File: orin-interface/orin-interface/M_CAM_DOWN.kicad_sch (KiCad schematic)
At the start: 19 parts, among them T5 749022310

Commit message: orin-interface: PoE channels, buses, 3V3 regulator, ERC fixes
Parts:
- C42, C43, C44, C45, C46, C47, C48, C49, C50, C51: footprint (none) -> Capacitor_SMD:C_0603_1608Metric_Pad1.08x0.95mm_HandSolder
- R31, R35, R39, R43, R53, R54, R55, R56: footprint (none) -> Resistor_SMD:R_0603_1608Metric_Pad0.98x0.95mm_HandSolder
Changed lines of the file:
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@@
 			)
 		)
-		(property "Footprint" ""
+		(property "Footprint" "Resistor_SMD:R_0603_1608Metric_Pad0.98x0.95mm_HandSolder"
 			(at 137.16 77.47 0)
 			(hide yes)
@@
 			)
 		)
-		(property "Footprint" ""
+		(property "Footprint" "Capacitor_SMD:C_0603_1608Metric_Pad1.08x0.95mm_HandSolder"
 			(at 101.6 83.82 0)
 			(hide yes)
@@
 			)
 		)
-		(property "Footprint" ""
+		(property "Footprint" "Capacitor_SMD:C_0603_1608Metric_Pad1.08x0.95mm_HandSolder"
 			(at 91.44 83.82 0)
 			(hide yes)
@@
 			)
 		)
-		(property "Footprint" ""
+		(property "Footprint" "Resistor_SMD:R_0603_1608Metric_Pad0.98x0.95mm_HandSolder"
 			(at 91.44 77.47 0)
 			(hide yes)
@@
 			)
 		)
-		(property "Footprint" ""
+		(property "Footprint" "Resistor_SMD:R_0603_1608Metric_Pad0.98x0.95mm_HandSolder"
 			(at 86.36 77.47 0)
 			(hide yes)
@@
 			)
 		)
-		(property "Footprint" ""
+		(property "Footprint" "Resistor_SMD:R_0603_1608Metric_Pad0.98x0.95mm_HandSolder"
 			(at 127 77.47 0)
 			(hide yes)
@@
 			)
 		)
-		(property "Footprint" ""
+		(property "Footprint" "Capacitor_SMD:C_0603_1608Metric_Pad1.08x0.95mm_HandSolder"
 			(at 134.62 91.44 0)
 			(hide yes)
@@
 			)
 		)
-		(property "Footprint" ""
+		(property "Footprint" "Capacitor_SMD:C_0603_1608Metric_Pad1.08x0.95mm_HandSolder"
 			(at 137.16 83.82 0)
 			(hide yes)
@@
 			)
 		)
-		(property "Footprint" ""
+		(property "Footprint" "Capacitor_SMD:C_0603_1608Metric_Pad1.08x0.95mm_HandSolder"
 			(at 127 83.82 0)
 			(hide yes)
@@
 			)
 		)
-		(property "Footprint" ""
+		(property "Footprint" "Capacitor_SMD:C_0603_1608Metric_Pad1.08x0.95mm_HandSolder"
 			(at 86.36 83.82 0)
 			(hide yes)
@@
 			)
 		)
-		(property "Footprint" ""
+		(property "Footprint" "Capacitor_SMD:C_0603_1608Metric_Pad1.08x0.95mm_HandSolder"
 			(at 96.52 83.82 0)
 			(hide yes)
@@
 			)
 		)
-		(property "Footprint" ""
+		(property "Footprint" "Capacitor_SMD:C_0603_1608Metric_Pad1.08x0.95mm_HandSolder"
 			(at 93.98 91.44 0)
 			(hide yes)
@@
 			)
 		)
-		(property "Footprint" ""
+		(property "Footprint" "Capacitor_SMD:C_0603_1608Metric_Pad1.08x0.95mm_HandSolder"
 			(at 132.08 83.82 0)
 			(hide yes)
@@
 			)
 		)
-		(property "Footprint" ""
+		(property "Footprint" "Capacitor_SMD:C_0603_1608Metric_Pad1.08x0.95mm_HandSolder"
 			(at 142.24 83.82 0)
 			(hide yes)
@@
 			)
 		)
-		(property "Footprint" ""
+		(property "Footprint" "Resistor_SMD:R_0603_1608Metric_Pad0.98x0.95mm_HandSolder"
 			(at 132.08 77.47 0)
 			(hide yes)
@@
 			)
 		)
-		(property "Footprint" ""
+		(property "Footprint" "Resistor_SMD:R_0603_1608Metric_Pad0.98x0.95mm_HandSolder"
 			(at 142.24 77.47 0)
 			(hide yes)
@@
 			)
 		)
-		(property "Footprint" ""
+		(property "Footprint" "Resistor_SMD:R_0603_1608Metric_Pad0.98x0.95mm_HandSolder"
 			(at 101.6 77.47 0)
 			(hide yes)
@@
 			)
 		)
-		(property "Footprint" ""
+		(property "Footprint" "Resistor_SMD:R_0603_1608Metric_Pad0.98x0.95mm_HandSolder"
 			(at 96.52 77.47 0)
 			(hide yes)

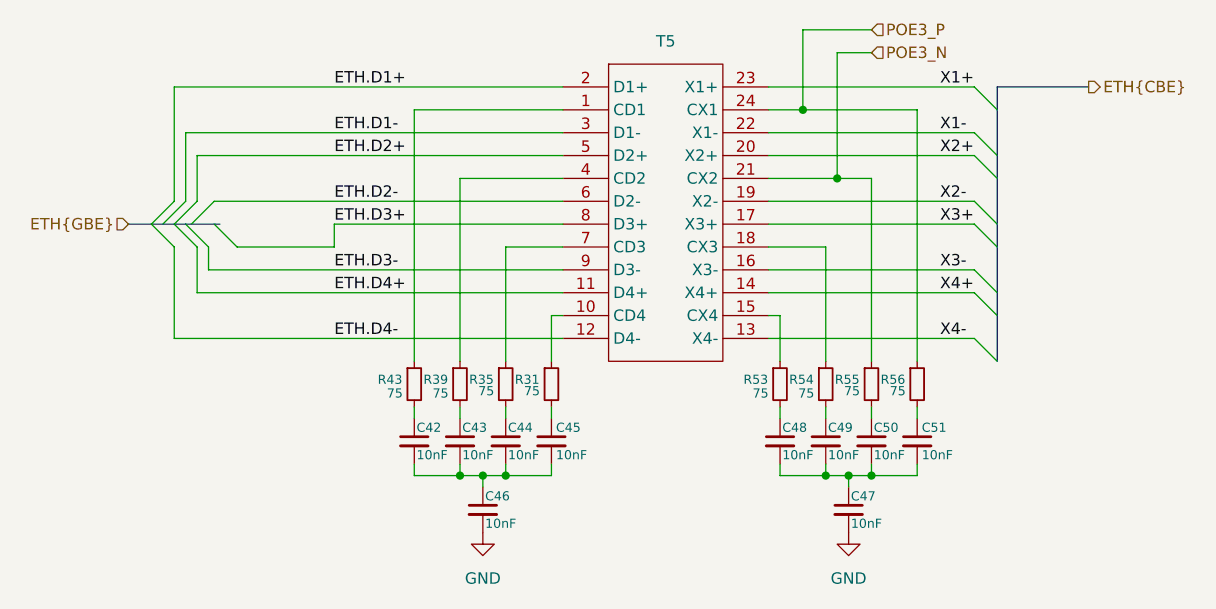
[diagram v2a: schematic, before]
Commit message: orin-interface: add ETH connector sheets and Mate-connectors footprint lib; update orin-bob
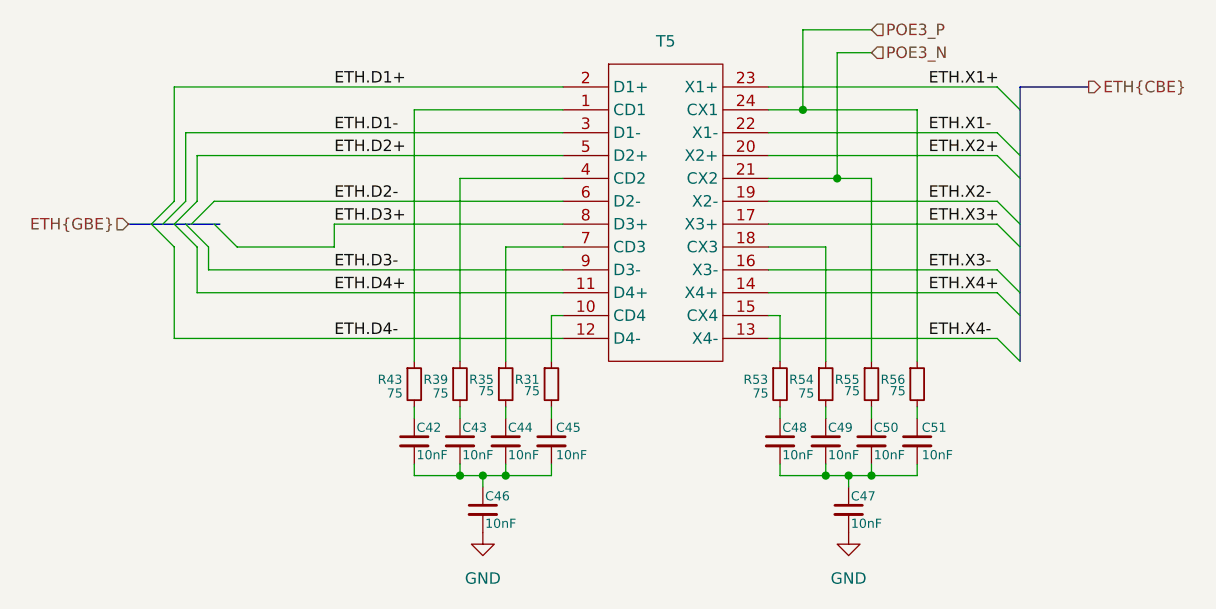
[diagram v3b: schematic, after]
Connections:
- net X1+ renamed ETH.X1+
- net X1- renamed ETH.X1-
- net X2+ renamed ETH.X2+
- net X2- renamed ETH.X2-
- net X3+ renamed ETH.X3+
- net X3- renamed ETH.X3-
- net X4+ renamed ETH.X4+
- net X4- renamed ETH.X4-
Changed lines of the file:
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@@
 	)
 	(bus_entry
-		(at 148.59 44.45)
-		(size 2.54 2.54)
-		(stroke
-			(width 0)
-			(type default)
-		)
-	)
-	(bus_entry
-		(at 148.59 67.31)
+		(at 151.13 44.45)
+		(size 2.54 2.54)
+		(stroke
+			(width 0)
+			(type default)
+		)
+	)
+	(bus_entry
+		(at 151.13 67.31)
 		(size 2.54 2.54)
 		(stroke
@@
 	)
 	(bus_entry
-		(at 148.59 52.07)
+		(at 151.13 52.07)
 		(size 2.54 2.54)
 		(stroke
@@
 	)
 	(bus_entry
-		(at 148.59 49.53)
-		(size 2.54 2.54)
-		(stroke
-			(width 0)
-			(type default)
-		)
-	)
-	(bus_entry
-		(at 148.59 72.39)
+		(at 151.13 49.53)
+		(size 2.54 2.54)
+		(stroke
+			(width 0)
+			(type default)
+		)
+	)
+	(bus_entry
+		(at 151.13 72.39)
 		(size 2.54 2.54)
 		(stroke
@@
 	)
 	(bus_entry
-		(at 148.59 57.15)
-		(size 2.54 2.54)
-		(stroke
-			(width 0)
-			(type default)
-		)
-	)
-	(bus_entry
-		(at 148.59 64.77)
+		(at 151.13 57.15)
+		(size 2.54 2.54)
+		(stroke
+			(width 0)
+			(type default)
+		)
+	)
+	(bus_entry
+		(at 151.13 64.77)
 		(size 2.54 2.54)
 		(stroke
@@
 	)
 	(bus_entry
-		(at 148.59 59.69)
+		(at 151.13 59.69)
 		(size 2.54 2.54)
 		(stroke
@@
 	(wire
 		(pts
-			(xy 125.73 44.45) (xy 148.59 44.45)
+			(xy 125.73 44.45) (xy 151.13 44.45)
 		)
 		(stroke
@@
 	(wire
 		(pts
-			(xy 125.73 72.39) (xy 148.59 72.39)
+			(xy 125.73 72.39) (xy 151.13 72.39)
 		)
 		(stroke
@@
 	(wire
 		(pts
-			(xy 125.73 49.53) (xy 148.59 49.53)
+			(xy 125.73 49.53) (xy 151.13 49.53)
 		)
 		(stroke
@@
 	(wire
 		(pts
-			(xy 125.73 67.31) (xy 148.59 67.31)
-		)
-		(stroke
-			(width 0)
-			(type default)
-		)
-	)
-	(wire
-		(pts
-			(xy 125.73 59.69) (xy 148.59 59.69)
+			(xy 125.73 67.31) (xy 151.13 67.31)
+		)
+		(stroke
+			(width 0)
+			(type default)
+		)
+	)
+	(wire
+		(pts
+			(xy 125.73 59.69) (xy 151.13 59.69)
 		)
 		(stroke
@@
 	(wire
 		(pts
-			(xy 125.73 57.15) (xy 148.59 57.15)
+			(xy 125.73 57.15) (xy 151.13 57.15)
 		)
 		(stroke
@@
 	(wire
 		(pts
-			(xy 125.73 64.77) (xy 148.59 64.77)
+			(xy 125.73 64.77) (xy 151.13 64.77)
 		)
 		(stroke
@@
 	(bus
 		(pts
-			(xy 151.13 44.45) (xy 161.29 44.45)
+			(xy 153.67 44.45) (xy 161.29 44.45)
 		)
 		(stroke
@@
 	(bus
 		(pts
-			(xy 151.13 44.45) (xy 151.13 74.93)
+			(xy 153.67 44.45) (xy 153.67 74.93)
 		)
 		(stroke
@@
 	(wire
 		(pts
-			(xy 125.73 52.07) (xy 148.59 52.07)
+			(xy 125.73 52.07) (xy 151.13 52.07)
 		)
 		(stroke
@@
 		)
 	)
-	(label "X1+"
-		(at 144.78 44.45 0)
+	(label "ETH.X1+"
+		(at 143.51 44.45 0)
 		(effects
 			(font
@@
 		)
 	)
-	(label "X1-"
-		(at 144.78 49.53 0)
+	(label "ETH.X1-"
+		(at 143.51 49.53 0)
 		(effects
 			(font
@@
 		)
 	)
-	(label "X3+"
-		(at 144.78 59.69 0)
-		(effects
-			(font
-				(size 1.27 1.27)
-			)
-			(justify left bottom)
-		)
-	)
-	(label "X4-"
-		(at 144.78 72.39 0)
+	(label "ETH.X3+"
+		(at 143.51 59.69 0)
+		(effects
+			(font
+				(size 1.27 1.27)
+			)
+			(justify left bottom)
+		)
+	)
+	(label "ETH.X4-"
+		(at 143.51 72.39 0)
 		(effects
 			(font
@@
 		)
 	)
-	(label "X2-"
-		(at 144.78 57.15 0)
+	(label "ETH.X2-"
+		(at 143.51 57.15 0)
 		(effects
 			(font
@@
 		)
 	)
-	(label "X2+"
-		(at 144.78 52.07 0)
-		(effects
-			(font
-				(size 1.27 1.27)
-			)
-			(justify left bottom)
-		)
-	)
-	(label "X3-"
-		(at 144.78 64.77 0)
-		(effects
-			(font
-				(size 1.27 1.27)
-			)
-			(justify left bottom)
-		)
-	)
-	(label "X4+"
-		(at 144.78 67.31 0)
-		(effects
-			(font
+	(label "ETH.X2+"
+		(at 143.51 52.07 0)
+		(effects
+			(font
+				(size 1.27 1.27)
+			)
+			(justify left bottom)
+		)
+	)
+	(label "ETH.X3-"
+		(at 143.51 64.77 0)
+		(effects
+			(font
+				(size 1.27 1.27)
+			)
+			(justify left bottom)
+		)
+	)
+	(label "ETH.X4+"
+		(at 143.51 67.31 0)
+		(effects
+			(font
